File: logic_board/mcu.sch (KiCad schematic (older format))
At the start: 19 parts, among them J1 SWD Interface, SW1 TL3315NF160Q, SW2 TL3315NF160Q, SW3 TL3315NF160Q, SW4 TL3315NF160Q, U1 STM32F302C8Tx, Y1 8 MHz

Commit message: Remove boot selection jumper. Add silk screen battery polarity indicator
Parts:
- removed JP1: Boot Mode, Pin_Headers:Pin_Header_Straight_1x02_Pitch2.54mm, symbol Device:Jumper
- removed R18: 100k, Resistors_SMD:R_0402, symbol Device:R
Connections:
- wire segments 107 -> 105
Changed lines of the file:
@@
 	4350 3200 4350 3150
 Wire Wire Line
-	4650 2450 4850 2450
+	4650 2450 4700 2450
 Wire Wire Line
 	8650 1950 8750 1950
@@
 NoConn ~ 5350 2250
 $Comp
-L Device:Jumper JP1
-U 1 1 5E366F3E
-P 3250 2650
-F 0 "JP1" H 3250 2914 50  0000 C CNN
-F 1 "Boot Mode" H 3250 2823 50  0000 C CNN
-F 2 "Pin_Headers:Pin_Header_Straight_1x02_Pitch2.54mm" H 3250 2650 50  0001 C CNN
-F 3 "~" H 3250 2650 50  0001 C CNN
-	1    3250 2650
-	1    0    0    -1
-$EndComp
-$Comp
-L power:GND #PWR05
-U 1 1 5E368029
-P 2750 2650
-F 0 "#PWR05" H 2750 2400 50  0001 C CNN
-F 1 "GND" V 2755 2522 50  0000 R CNN
-F 2 "" H 2750 2650 50  0001 C CNN
-F 3 "" H 2750 2650 50  0001 C CNN
-	1    2750 2650
-	0    1    1    0
-$EndComp
-$Comp
-L Device:R R18
-U 1 1 5E36CB47
-P 3650 2350
-F 0 "R18" H 3720 2396 50  0000 L CNN
-F 1 "100k" H 3720 2305 50  0000 L CNN
-F 2 "Resistors_SMD:R_0402" V 3580 2350 50  0001 C CNN
-F 3 "~" H 3650 2350 50  0001 C CNN
-	1    3650 2350
-	1    0    0    -1
-$EndComp
-$Comp
-L power:+3V3 #PWR042
-U 1 1 5E36D529
-P 3650 2050
-F 0 "#PWR042" H 3650 1900 50  0001 C CNN
-F 1 "+3V3" H 3665 2223 50  0000 C CNN
-F 2 "" H 3650 2050 50  0001 C CNN
-F 3 "" H 3650 2050 50  0001 C CNN
-	1    3650 2050
-	1    0    0    -1
-$EndComp
-Wire Wire Line
-	3550 2650 3650 2650
-Wire Wire Line
-	3650 2650 3650 2500
-Wire Wire Line
-	3650 2200 3650 2050
-Wire Wire Line
-	3650 2650 4850 2650
-Connection ~ 3650 2650
-Wire Wire Line
-	2750 2650 2950 2650
-$Comp
 L Switch:SW_Push SW4
 U 1 1 5E4374E4
@@
 Wire Wire Line
 	7950 3050 8250 3050
+Wire Wire Line
+	4850 2650 4700 2650
+Wire Wire Line
+	4700 2650 4700 2450
+Connection ~ 4700 2450
+Wire Wire Line
+	4700 2450 4850 2450
 $EndSCHEMATC

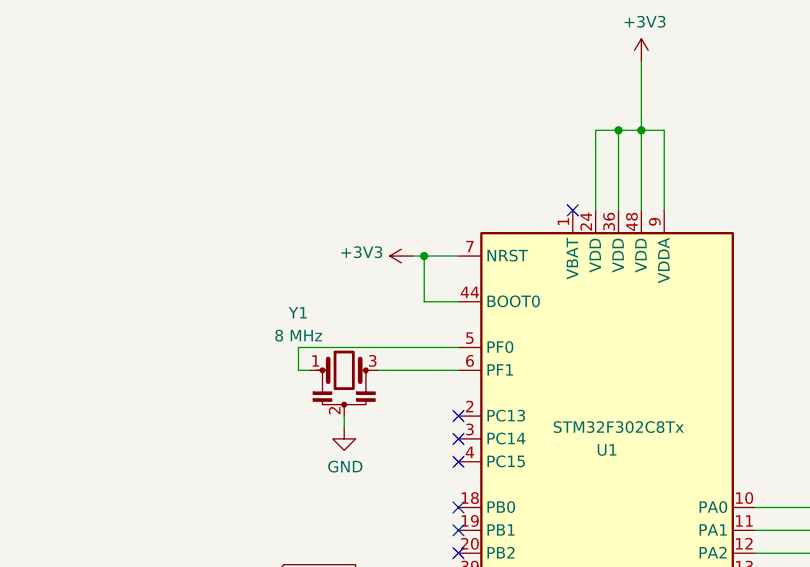
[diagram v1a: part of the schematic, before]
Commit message: Pull BOOT0 pin down by default to boot from flash
Also thickened some power traces to MPU.
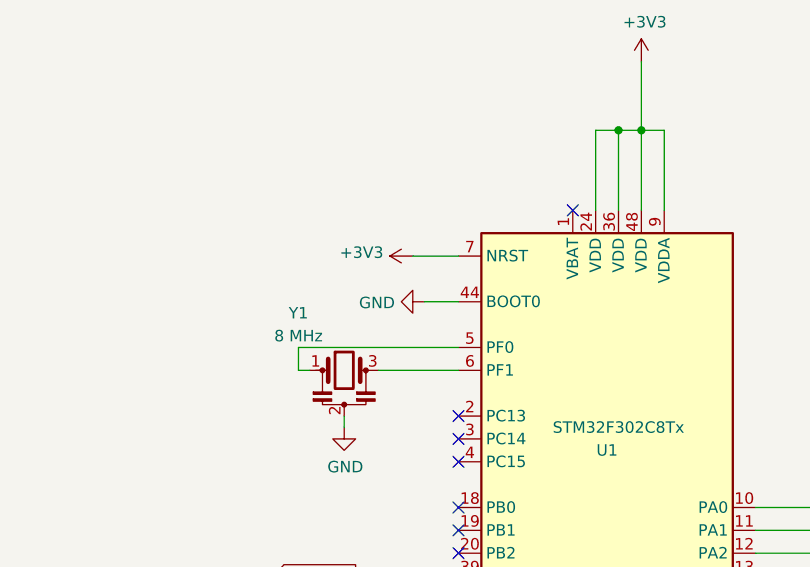
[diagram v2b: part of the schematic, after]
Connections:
- net +3V3: no longer U1.44 (BOOT0)
- net GND: now also U1.44 (BOOT0)
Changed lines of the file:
@@
 	4350 3200 4350 3150
-Wire Wire Line
-	4650 2450 4700 2450
 Wire Wire Line
 	8650 1950 8750 1950
@@
 	4850 2650 4700 2650
 Wire Wire Line
-	4700 2650 4700 2450
-Connection ~ 4700 2450
-Wire Wire Line
-	4700 2450 4850 2450
+	4650 2450 4850 2450
+$Comp
+L power:GND #PWR?
+U 1 1 5E360F12
+P 4700 2650
+F 0 "#PWR?" H 4700 2400 50  0001 C CNN
+F 1 "GND" V 4705 2522 50  0000 R CNN
+F 2 "" H 4700 2650 50  0001 C CNN
+F 3 "" H 4700 2650 50  0001 C CNN
+	1    4700 2650
+	0    1    1    0
+$EndComp
 $EndSCHEMATC

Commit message: Minor tweaks
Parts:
- SW1: Name Volume Up -> Volume Down
- SW2: Field4 Volume Down -> Volume Up
- SW3: Name Next Fx -> Metronome
- SW4: Name Metronome -> Switch Effect
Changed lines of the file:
@@
 encoding utf-8
 Sheet 2 4
-Title "MCU"
-Date "2020-01-26"
+Title "Microcontroller"
+Date "2020-02-02"
 Rev "1.0"
 Comp ""
@@
 F 2 "custom_footprints:TL3315NF160Q_Tactile_Switch" H 8450 3250 50  0001 C CNN
 F 3 "http://spec_sheets.e-switch.com/specs/P010337.pdf" H 8450 3250 50  0001 C CNN
-F 4 "Metronome" H 8800 3150 50  0000 C CNN "Name"
+F 4 "Switch Effect" H 8800 3150 50  0000 C CNN "Name"
 	1    8450 3050
 	1    0    0    -1
@@
 F 2 "custom_footprints:TL3315NF160Q_Tactile_Switch" H 8450 2150 50  0001 C CNN
 F 3 "http://spec_sheets.e-switch.com/specs/P010337.pdf" H 8450 2150 50  0001 C CNN
-F 4 "Volume Up" H 8800 2050 50  0000 C CNN "Name"
+F 4 "Volume Down" H 8800 2050 50  0000 C CNN "Name"
 	1    8450 1950
 	1    0    0    -1
@@
 F 2 "custom_footprints:TL3315NF160Q_Tactile_Switch" H 8450 2900 50  0001 C CNN
 F 3 "http://spec_sheets.e-switch.com/specs/P010337.pdf" H 8450 2900 50  0001 C CNN
-F 4 "Next Fx" H 8750 2750 50  0000 C CNN "Name"
+F 4 "Metronome" H 8750 2750 50  0000 C CNN "Name"
 	1    8450 2700
 	1    0    0    -1
@@
 F 2 "custom_footprints:TL3315NF160Q_Tactile_Switch" H 8450 2550 50  0001 C CNN
 F 3 "http://spec_sheets.e-switch.com/specs/P010337.pdf" H 8450 2550 50  0001 C CNN
-F 4 "Volume Down" H 8850 2450 50  0000 C CNN "Field4"
+F 4 "Volume Up" H 8850 2450 50  0000 C CNN "Field4"
 	1    8450 2350
 	1    0    0    -1

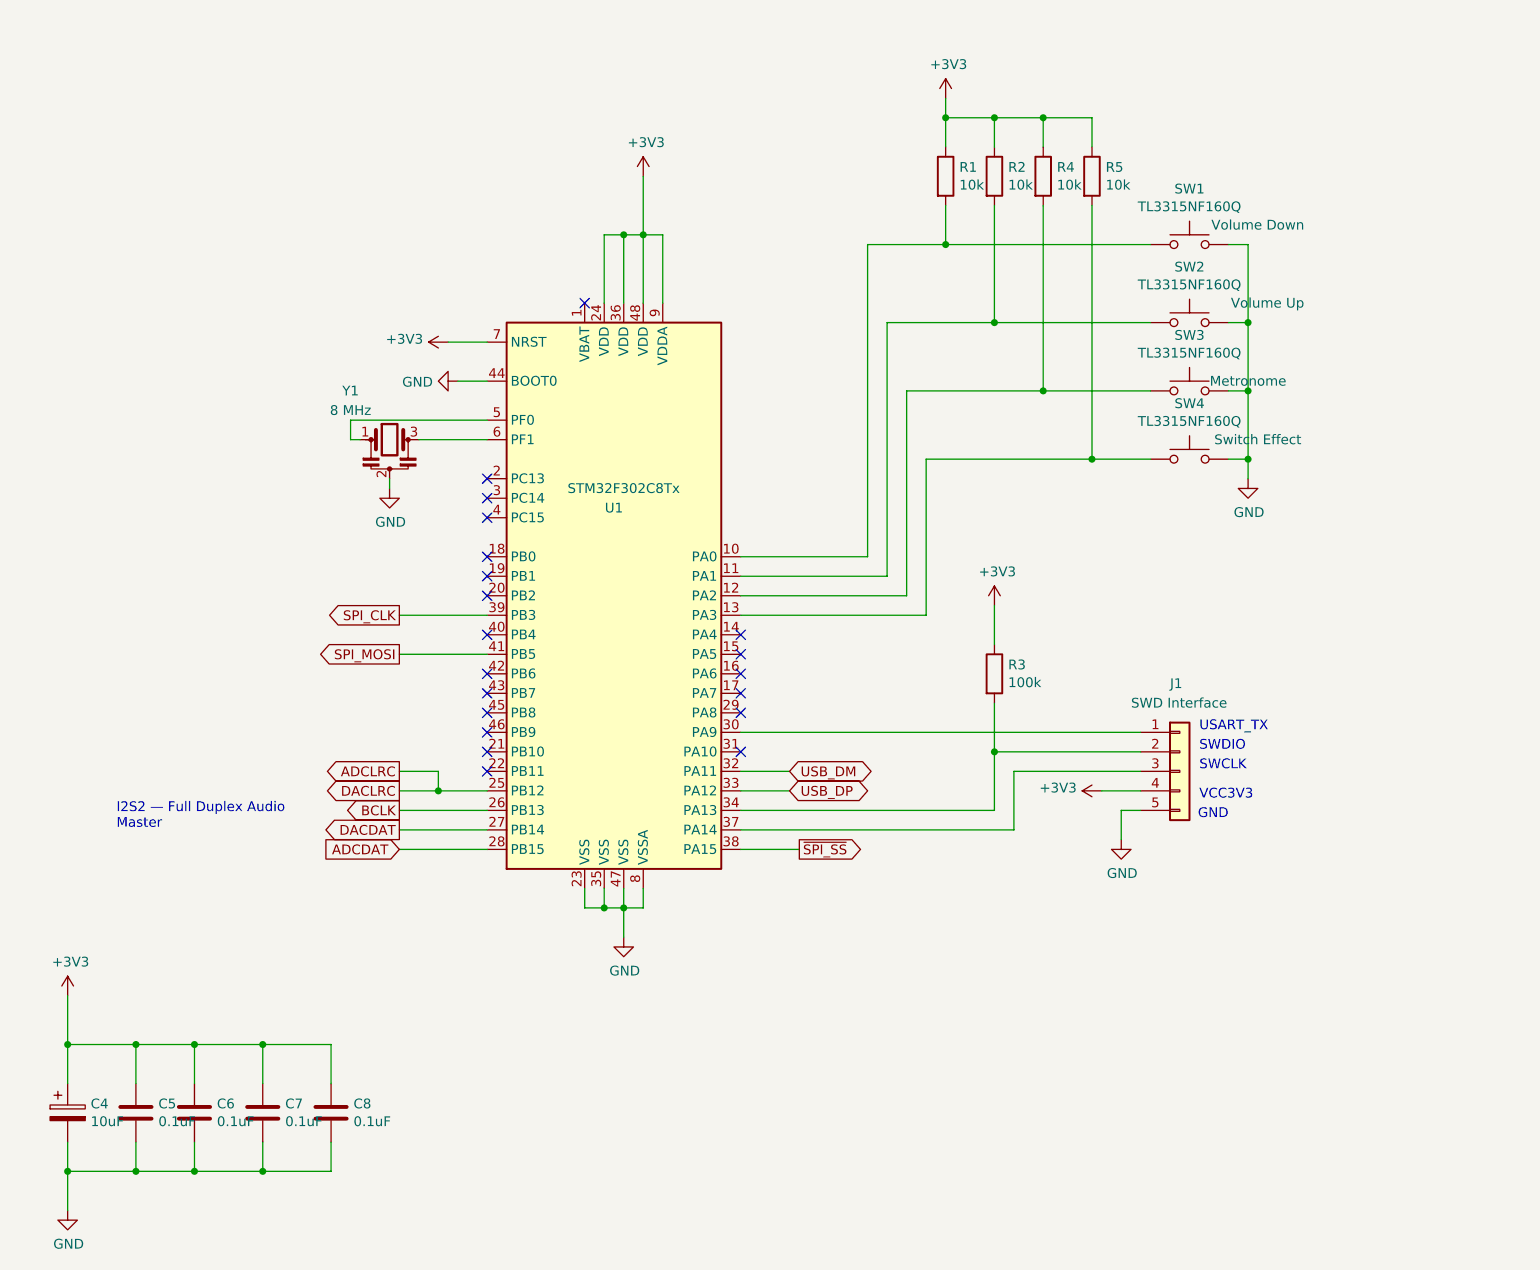
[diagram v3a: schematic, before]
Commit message: Switch to a microcontroller with more SRAM
This is necessary to enable some effects like reverb and echo.
This part has a similar pinout, but not exactly the same, which required some layout
changes.
I also took this opportuntity to move the serial pins to a separate header with its
own ground, which makes connecting a serial debugger and SWD interface at the same
time easier.
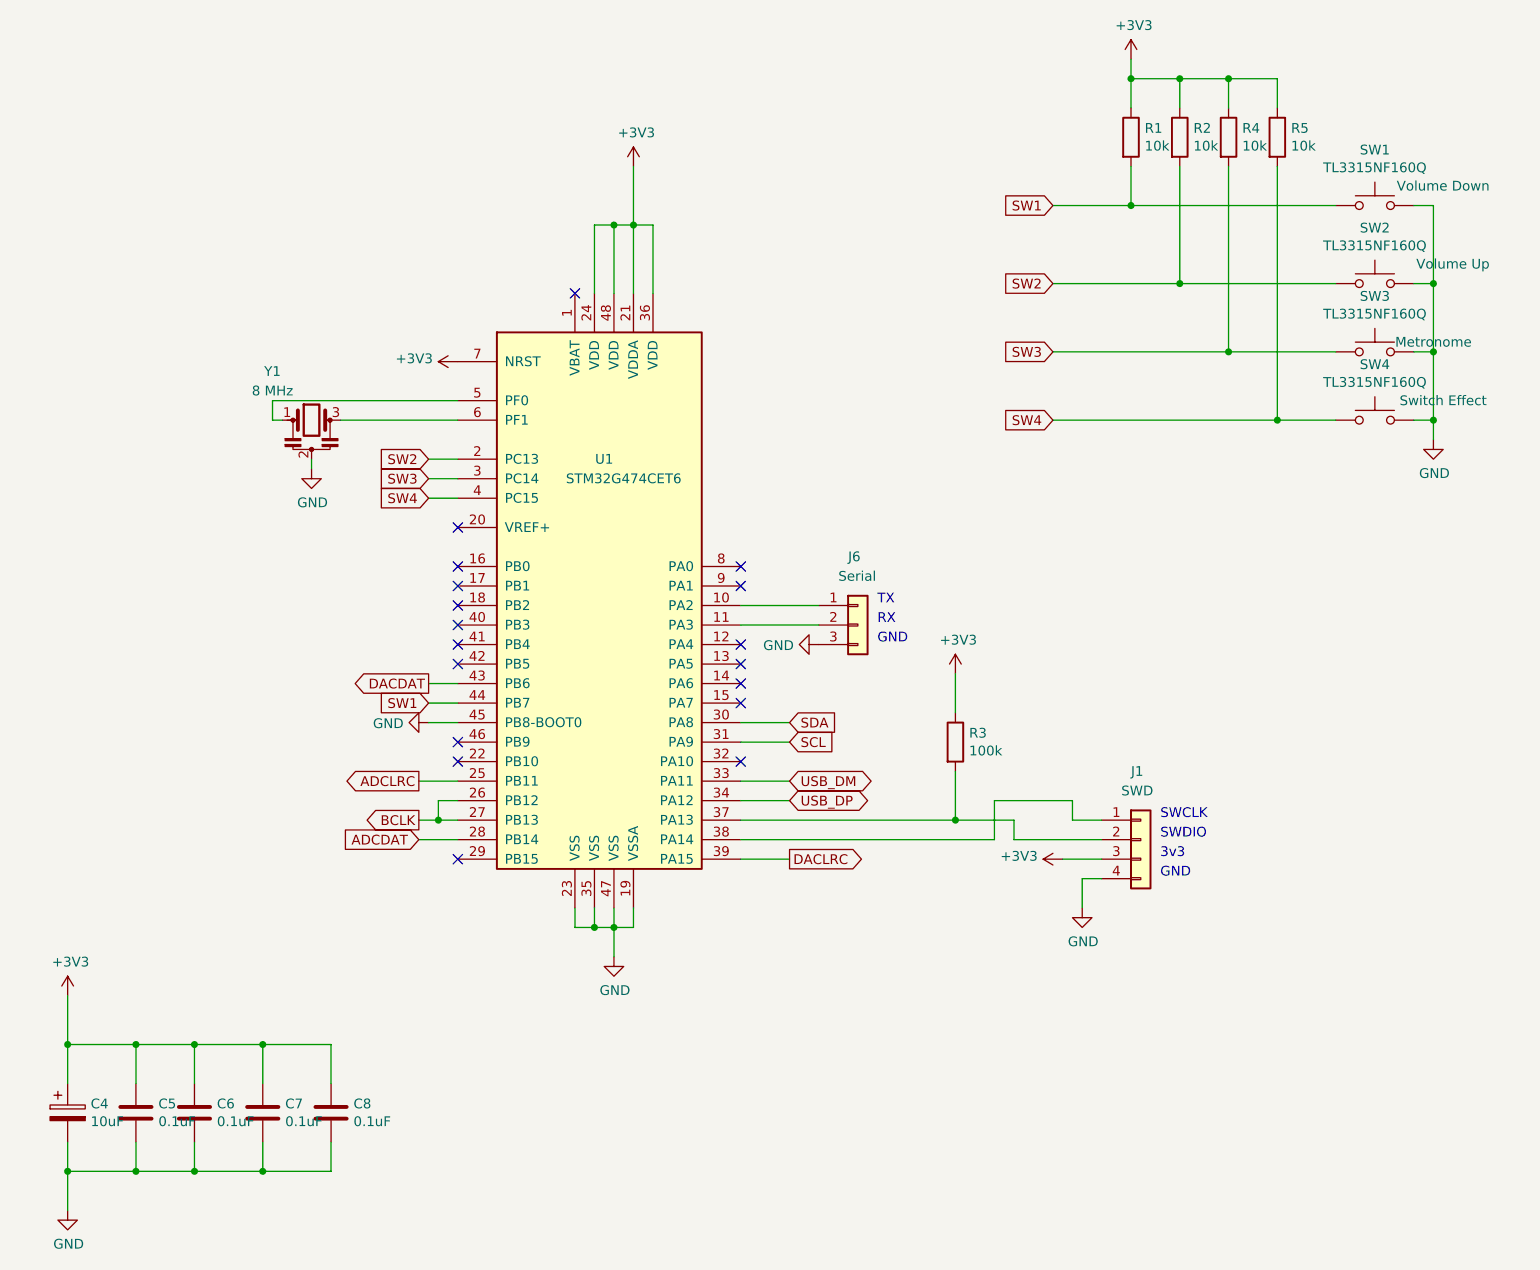
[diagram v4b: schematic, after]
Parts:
- removed J1: SWD Interface, Pin_Headers:Pin_Header_Straight_1x05_Pitch2.54mm, symbol Connector_Generic:Conn_01x05
- removed U1: STM32F302C8Tx, Housings_QFP:LQFP-48_7x7mm_Pitch0.5mm, symbol MCU_ST_STM32F3:STM32F302C8Tx
- added J1: SWD, Pin_Headers:Pin_Header_Straight_1x04_Pitch2.54mm, symbol Connector_Generic:Conn_01x04
- added J6: Serial, Pin_Headers:Pin_Header_Straight_1x03_Pitch2.54mm, symbol Connector_Generic:Conn_01x03
- added U1: STM32G474CET6, Housings_QFP:LQFP-48_7x7mm_Pitch0.5mm, symbol parts:STM32G474CET6
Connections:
- net +3V3: now also J1.3 (Pin_3), U1.21 (VDDA), U1.24 (VDD), U1.36 (VDD), U1.48 (VDD), U1.7 (NRST)
- net ADCDAT: now also U1.28 (PB14)
- net ADCLRC: now also U1.25 (PB11)
- net BCLK: now also U1.26 (PB12), U1.27 (PB13)
- net DACDAT: now also U1.43 (PB6)
- net GND: now also J1.4 (Pin_4), J6.3 (Pin_3), U1.19 (VSSA), U1.23 (VSS), U1.35 (VSS), U1.45 (PB8-BOOT0), U1.47 (VSS)
- net USB_DM: now also U1.33 (PA11)
- net USB_DP: now also U1.34 (PA12)
- net SW1: now reaches R1.2, SW1.1
- net SW1: now also U1.44 (PB7)
- net SW2: now reaches R2.2, SW2.1
- net SW2: now also U1.2 (PC13)
- net SW3: now reaches R4.2, SW3.1
- net SW3: now also U1.3 (PC14)
- net SW4: now reaches R5.2, SW4.1
- net SW4: now also U1.4 (PC15)
- net at R3.2: now also J1.2 (Pin_2), U1.37 (PA13)
- net at Y1.1: now also U1.5 (PF0)
- net at Y1.3: now also U1.6 (PF1)
- new net: J6.1 (Pin_1), U1.10 (PA2)
- new net: J6.2 (Pin_2), U1.11 (PA3)
- new net: J1.1 (Pin_1), U1.38 (PA14)
- new net DACLRC: U1.39 (PA15)
- new net SCL: U1.31 (PA9)
- new net SDA: U1.30 (PA8)
- no-connect marks 20 -> 18
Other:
- note added: "3v3"
- note added: "GND"
- note added: "RX"
- note added: "TX"
- note removed: "GND\n"
- note removed: "I2S2 — Full Duplex Audio\nMaster"
- note removed: "USART_TX"
- note removed: "VCC3V3"
- moved on the sheet: R1, R2, R3, R4, R5, SW1, SW2, SW3, SW4, Y1

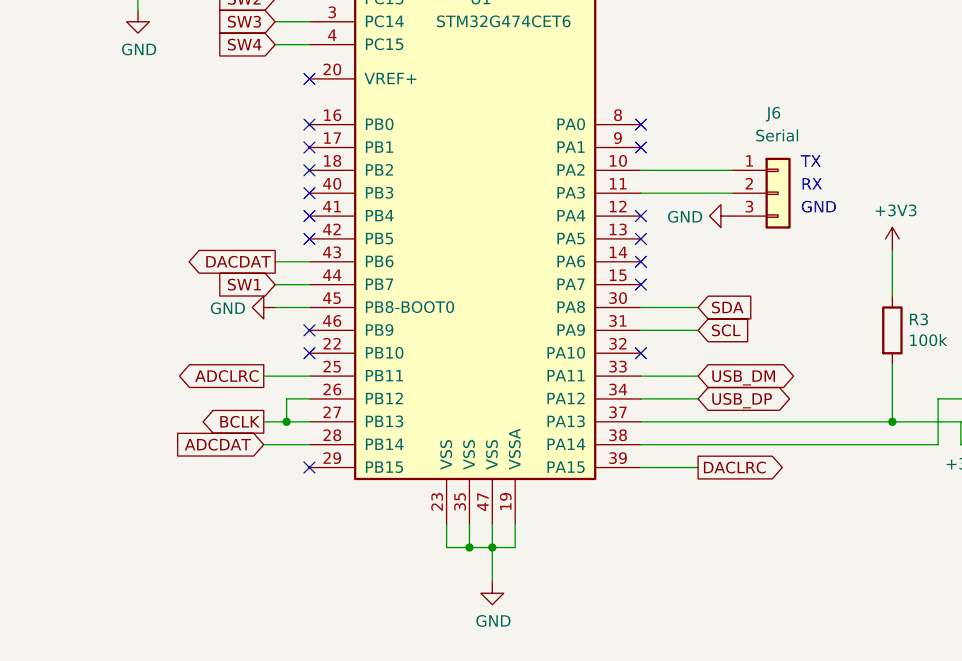
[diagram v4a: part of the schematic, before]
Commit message: Fix a few incorrect MCU pin connections from last change.
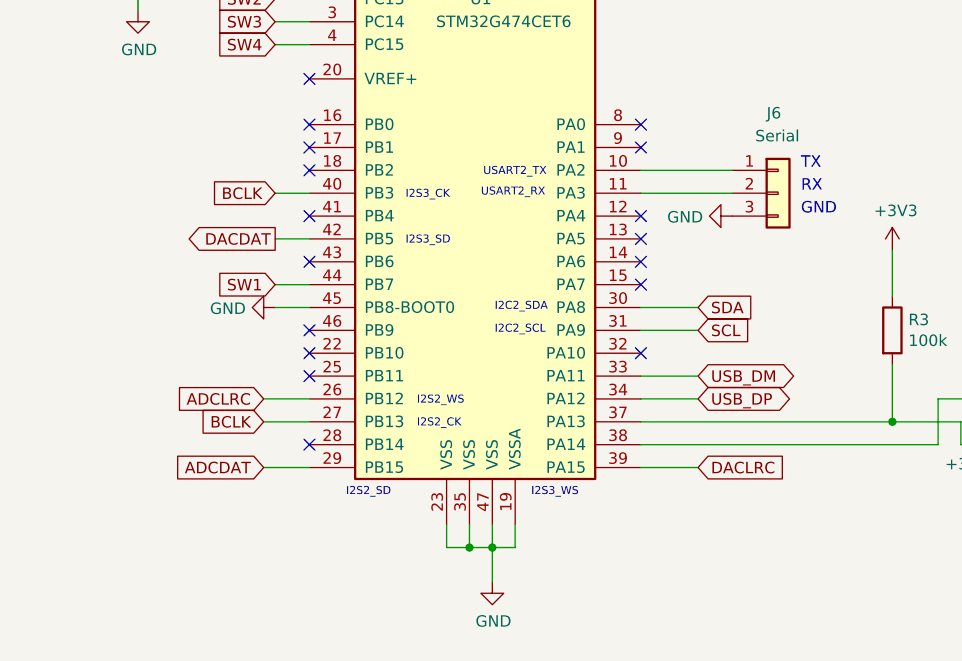
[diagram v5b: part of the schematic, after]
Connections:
- net ADCDAT: now also U1.29 (PB15); no longer U1.28 (PB14)
- net ADCLRC: now also U1.26 (PB12); no longer U1.25 (PB11)
- net BCLK: now also U1.40 (PB3); no longer U1.26 (PB12)
- net DACDAT: now also U1.42 (PB5); no longer U1.43 (PB6)
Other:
- note added: "I2C2_SCL"
- note added: "I2C2_SDA"
- note added: "I2S2_CK"
- note added: "I2S2_SD"
- note added: "I2S2_WS"
- note added: "I2S3_CK"
- note added: "I2S3_SD"
- note added: "I2S3_WS"
- note added: "USART2_RX"
- note added: "USART2_TX"
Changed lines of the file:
@@
 	0    -1   -1   0
 $EndComp
-Text GLabel 4500 4900 0    50   Output ~ 0
+Text GLabel 4500 4900 0    50   Input ~ 0
 BCLK
-Text GLabel 4500 4700 0    50   Output ~ 0
+Text GLabel 4500 4800 0    50   Input ~ 0
 ADCLRC
-Text GLabel 6400 5100 2    50   Output ~ 0
+Text GLabel 6400 5100 2    50   Input ~ 0
 DACLRC
-Text GLabel 4500 5000 0    50   Input ~ 0
+Text GLabel 4500 5100 0    50   Input ~ 0
 ADCDAT
-Text GLabel 4550 4200 0    50   Output ~ 0
+Text GLabel 4550 4100 0    50   Output ~ 0
 DACDAT
 $Comp
@@
 $EndComp
 Wire Wire Line
-	4500 4900 4600 4900
-Wire Wire Line
-	4700 4800 4600 4800
-Wire Wire Line
-	4600 4800 4600 4900
-Connection ~ 4600 4900
-Wire Wire Line
-	4600 4900 4700 4900
-Wire Wire Line
-	4500 5000 4700 5000
-Wire Wire Line
-	4550 4200 4700 4200
-Wire Wire Line
 	6150 5100 6400 5100
-Wire Wire Line
-	4500 4700 4700 4700
 Wire Wire Line
 	6150 4700 6400 4700
@@
 NoConn ~ 4700 3700
 NoConn ~ 4700 3800
-NoConn ~ 4700 3900
 NoConn ~ 4700 4000
-NoConn ~ 4700 4100
 NoConn ~ 4700 4500
 NoConn ~ 4700 4600
-NoConn ~ 4700 5100
+NoConn ~ 4700 5000
 NoConn ~ 6150 3600
 NoConn ~ 6150 3700
@@
 Text Notes 6850 4000 0    50   ~ 0
 GND
+Wire Wire Line
+	4550 4100 4700 4100
+NoConn ~ 4700 4200
+Wire Wire Line
+	4500 4900 4700 4900
+Text GLabel 4550 3900 0    50   Input ~ 0
+BCLK
+Wire Wire Line
+	4550 3900 4700 3900
+Text Notes 5670 5230 0    35   ~ 0
+I2S3_WS
+Wire Wire Line
+	4500 5100 4700 5100
+Text Notes 4860 5230 0    35   ~ 0
+I2S2_SD
+NoConn ~ 4700 4700
+Wire Wire Line
+	4500 4800 4700 4800
+Text Notes 5170 4930 0    35   ~ 0
+I2S2_CK
+Text Notes 5170 4830 0    35   ~ 0
+I2S2_WS
+Text Notes 5120 4130 0    35   ~ 0
+I2S3_SD
+Text Notes 5120 3930 0    35   ~ 0
+I2S3_CK
+Text Notes 5460 3830 0    35   ~ 0
+USART2_TX
+Text Notes 5450 3920 0    35   ~ 0
+USART2_RX
+Text Notes 5510 4420 0    35   ~ 0
+I2C2_SDA
+Text Notes 5510 4520 0    35   ~ 0
+I2C2_SCL
 $EndSCHEMATC

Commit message: Add blinkenlights for debugging
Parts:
- added D3: Debug, LEDs:LED_0603_HandSoldering, symbol Device:LED
- added R18: 1.5k, Resistors_SMD:R_0402, symbol Device:R
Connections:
- net GND: now also R18.2
- net at U1.25 (PB11): now also D3.2 (A)
- new net: D3.1 (K), R18.1
- no-connect marks 18 -> 17
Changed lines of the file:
@@
 Text Notes 4860 5230 0    35   ~ 0
 I2S2_SD
-NoConn ~ 4700 4700
 Wire Wire Line
 	4500 4800 4700 4800
@@
 Text Notes 5510 4520 0    35   ~ 0
 I2C2_SCL
+$Comp
+L Device:LED D3
+U 1 1 5E4009C6
+P 3950 4700
+F 0 "D3" H 3943 4916 50  0000 C CNN
+F 1 "Debug" H 3943 4825 50  0000 C CNN
+F 2 "LEDs:LED_0603_HandSoldering" H 3950 4700 50  0001 C CNN
+F 3 "~" H 3950 4700 50  0001 C CNN
+	1    3950 4700
+	1    0    0    -1
+$EndComp
+Wire Wire Line
+	4100 4700 4700 4700
+$Comp
+L Device:R R18
+U 1 1 5E4050CB
+P 3500 4700
+F 0 "R18" V 3293 4700 50  0000 C CNN
+F 1 "1.5k" V 3384 4700 50  0000 C CNN
+F 2 "Resistors_SMD:R_0402" V 3430 4700 50  0001 C CNN
+F 3 "~" H 3500 4700 50  0001 C CNN
+	1    3500 4700
+	0    1    1    0
+$EndComp
+$Comp
+L power:GND #PWR05
+U 1 1 5E405DDC
+P 3200 4700
+F 0 "#PWR05" H 3200 4450 50  0001 C CNN
+F 1 "GND" V 3205 4572 50  0000 R CNN
+F 2 "" H 3200 4700 50  0001 C CNN
+F 3 "" H 3200 4700 50  0001 C CNN
+	1    3200 4700
+	0    1    1    0
+$EndComp
+Wire Wire Line
+	3200 4700 3350 4700
+Wire Wire Line
+	3650 4700 3800 4700
 $EndSCHEMATC
